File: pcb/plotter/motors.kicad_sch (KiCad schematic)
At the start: 22 parts, among them J6 Barrel_Jack_Switch, J8 Motor2, J9 Motor1, SW2 SW_SPDT, U2 bigtreetech-tmc2130, U3 bigtreetech-tmc2130, U5 MPRB2405S-6W

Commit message: PCB and 3d model. Still work in progress.
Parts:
- removed F1: Fuse, Fuse:Fuseholder_Cylinder-5x20mm_Bulgin_FX0456_Vertical_Closed, symbol Device:Fuse
- added F1: Polyfuse, Fuse:Fuse_1812_4532Metric, symbol Device:Polyfuse
- C29, C35, C37: footprint Capacitor_THT:CP_Radial_D13.0mm_P5.00mm -> Capacitor_SMD:CP_Elec_8x10
- J6: footprint Connector_BarrelJack:BarrelJack_Horizontal -> iwasz:BarrelJack_Horizontal
- J8, J9: footprint Connector_PinHeader_2.54mm:PinHeader_1x04_P2.54mm_Vertical -> Connector_JST:JST_PH_B4B-PH-K_1x04_P2.00mm_Vertical
- SW2: footprint Button_Switch_THT:SW_CuK_OS102011MA1QN1_SPDT_Angled -> iwasz:MFP 201 NR_copy
- U2, U3: footprint Module:Pololu_Breakout-16_15.2x20.3mm -> iwasz:Pololu_Breakout-16_15.2x20.3mm
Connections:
- net VDD is gone; now on net +5V: C2.2, C3.2, C30.2, C31.2, U2.2 (VDD), U3.2 (VDD)
- net +24V: now also F1.1
- net at C37.1, U5.2 (Vin): now also F1.2
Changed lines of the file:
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@@
     (pin "1")
   )
-  (symbol (lib_id "power:VDD") (at 118.745 52.07 0) (unit 1)
-    (in_bom yes) (on_board yes) (fields_autoplaced)
-    (property "Reference" "#PWR0107" (id 0) (at 118.745 55.88 0)
-      (effects (font (size 1.27 1.27)) hide)
-    )
-    (property "Value" "VDD" (id 1) (at 120.1421 51.4695 0)
+  (symbol (lib_id "power:+5V") (at 118.745 52.07 0) (unit 1)
+    (in_bom yes) (on_board yes) (fields_autoplaced)
+    (property "Reference" "#PWR?" (id 0) (at 118.745 55.88 0)
+      (effects (font (size 1.27 1.27)) hide)
+    )
+    (property "Value" "+5V" (id 1) (at 120.1421 51.4695 0)
       (effects (font (size 1.27 1.27)) (justify left))
     )
@@
     (pin "1")
   )
-  (symbol (lib_id "power:VDD") (at 173.355 52.07 0) (unit 1)
-    (in_bom yes) (on_board yes) (fields_autoplaced)
-    (property "Reference" "#PWR0104" (id 0) (at 173.355 55.88 0)
-      (effects (font (size 1.27 1.27)) hide)
-    )
-    (property "Value" "VDD" (id 1) (at 174.7521 51.4695 0)
+  (symbol (lib_id "power:+5V") (at 173.355 52.07 0) (unit 1)
+    (in_bom yes) (on_board yes) (fields_autoplaced)
+    (property "Reference" "#PWR?" (id 0) (at 173.355 55.88 0)
+      (effects (font (size 1.27 1.27)) hide)
+    )
+    (property "Value" "+5V" (id 1) (at 174.7521 51.4695 0)
       (effects (font (size 1.27 1.27)) (justify left))
     )
@@
     (pin "1")
   )
-  (symbol (lib_id "Device:Fuse") (at 104.14 166.37 90) (unit 1)
-    (in_bom yes) (on_board yes) (fields_autoplaced)
-    (property "Reference" "F1" (id 0) (at 104.14 161.6414 90))
-    (property "Value" "Fuse" (id 1) (at 104.14 164.4165 90))
-    (property "Footprint" "Fuse:Fuseholder_Cylinder-5x20mm_Bulgin_FX0456_Vertical_Closed" (id 2) (at 104.14 168.148 90)
-      (effects (font (size 1.27 1.27)) hide)
+  (symbol (lib_id "Device:Polyfuse") (at 104.14 166.37 90) (unit 1)
+    (in_bom yes) (on_board yes) (fields_autoplaced)
+    (property "Reference" "F1" (id 0) (at 104.14 161.0064 90))
+    (property "Value" "Polyfuse" (id 1) (at 104.14 163.7815 90))
+    (property "Footprint" "Fuse:Fuse_1812_4532Metric" (id 2) (at 109.22 165.1 0)
+      (effects (font (size 1.27 1.27)) (justify left) hide)
     )
     (property "Datasheet" "~" (id 3) (at 104.14 166.37 0)
@@
       (effects (font (size 1.27 1.27)) (justify left))
     )
-    (property "Footprint" "Capacitor_THT:CP_Radial_D13.0mm_P5.00mm" (id 2) (at 112.0902 175.26 0)
+    (property "Footprint" "Capacitor_SMD:CP_Elec_8x10" (id 2) (at 112.0902 175.26 0)
       (effects (font (size 1.27 1.27)) hide)
     )
@@
       (effects (font (size 1.27 1.27)) (justify left))
     )
-    (property "Footprint" "Capacitor_THT:CP_Radial_D13.0mm_P5.00mm" (id 2) (at 152.7302 64.135 0)
+    (property "Footprint" "Capacitor_SMD:CP_Elec_8x10" (id 2) (at 152.7302 64.135 0)
       (effects (font (size 1.27 1.27)) hide)
     )
@@
       (effects (font (size 1.27 1.27)) (justify left))
     )
-    (property "Footprint" "Capacitor_THT:CP_Radial_D13.0mm_P5.00mm" (id 2) (at 207.3402 64.135 0)
+    (property "Footprint" "Capacitor_SMD:CP_Elec_8x10" (id 2) (at 207.3402 64.135 0)
       (effects (font (size 1.27 1.27)) hide)
     )
@@
       (effects (font (size 1.27 1.27)) (justify right))
     )
-    (property "Footprint" "Connector_PinHeader_2.54mm:PinHeader_1x04_P2.54mm_Vertical" (id 2) (at 139.065 89.535 0)
+    (property "Footprint" "Connector_JST:JST_PH_B4B-PH-K_1x04_P2.00mm_Vertical" (id 2) (at 139.065 89.535 0)
       (effects (font (size 1.27 1.27)) hide)
     )
@@
       (effects (font (size 1.27 1.27)) (justify right))
     )
-    (property "Footprint" "Connector_PinHeader_2.54mm:PinHeader_1x04_P2.54mm_Vertical" (id 2) (at 193.675 89.535 0)
+    (property "Footprint" "Connector_JST:JST_PH_B4B-PH-K_1x04_P2.00mm_Vertical" (id 2) (at 193.675 89.535 0)
       (effects (font (size 1.27 1.27)) hide)
     )
@@
     (property "Reference" "SW2" (id 0) (at 59.69 156.9424 0))
     (property "Value" "SW_SPDT" (id 1) (at 59.69 159.7175 0))
-    (property "Footprint" "Button_Switch_THT:SW_CuK_OS102011MA1QN1_SPDT_Angled" (id 2) (at 59.69 163.83 0)
+    (property "Footprint" "iwasz:MFP 201 NR_copy" (id 2) (at 59.69 163.83 0)
       (effects (font (size 1.27 1.27)) hide)
     )
@@
     (property "Reference" "J6" (id 0) (at 42.672 158.5934 0))
     (property "Value" "Barrel_Jack_Switch" (id 1) (at 42.672 161.3685 0))
-    (property "Footprint" "Connector_BarrelJack:BarrelJack_Horizontal" (id 2) (at 42.545 167.386 0)
+    (property "Footprint" "iwasz:BarrelJack_Horizontal" (id 2) (at 42.545 167.386 0)
       (effects (font (size 1.27 1.27)) hide)
     )
@@
     (property "Reference" "U2" (id 0) (at 120.015 64.9944 0))
     (property "Value" "bigtreetech-tmc2130" (id 1) (at 120.015 67.7695 0))
-    (property "Footprint" "Module:Pololu_Breakout-16_15.2x20.3mm" (id 2) (at 120.015 88.265 0)
+    (property "Footprint" "iwasz:Pololu_Breakout-16_15.2x20.3mm" (id 2) (at 120.015 88.265 0)
       (effects (font (size 1.27 1.27)) hide)
     )
@@
     (property "Reference" "U3" (id 0) (at 174.625 64.9944 0))
     (property "Value" "bigtreetech-tmc2130" (id 1) (at 174.625 67.7695 0))
-    (property "Footprint" "Module:Pololu_Breakout-16_15.2x20.3mm" (id 2) (at 174.625 88.265 0)
-      (effects (font (size 1.27 1.27)) hide)
-    )
+    (property "Footprint" "iwasz:Pololu_Breakout-16_15.2x20.3mm" (id 2) (at 174.625 88.265 0)
+      (effects (font (size 1.27 1.27)) hide)
+    )

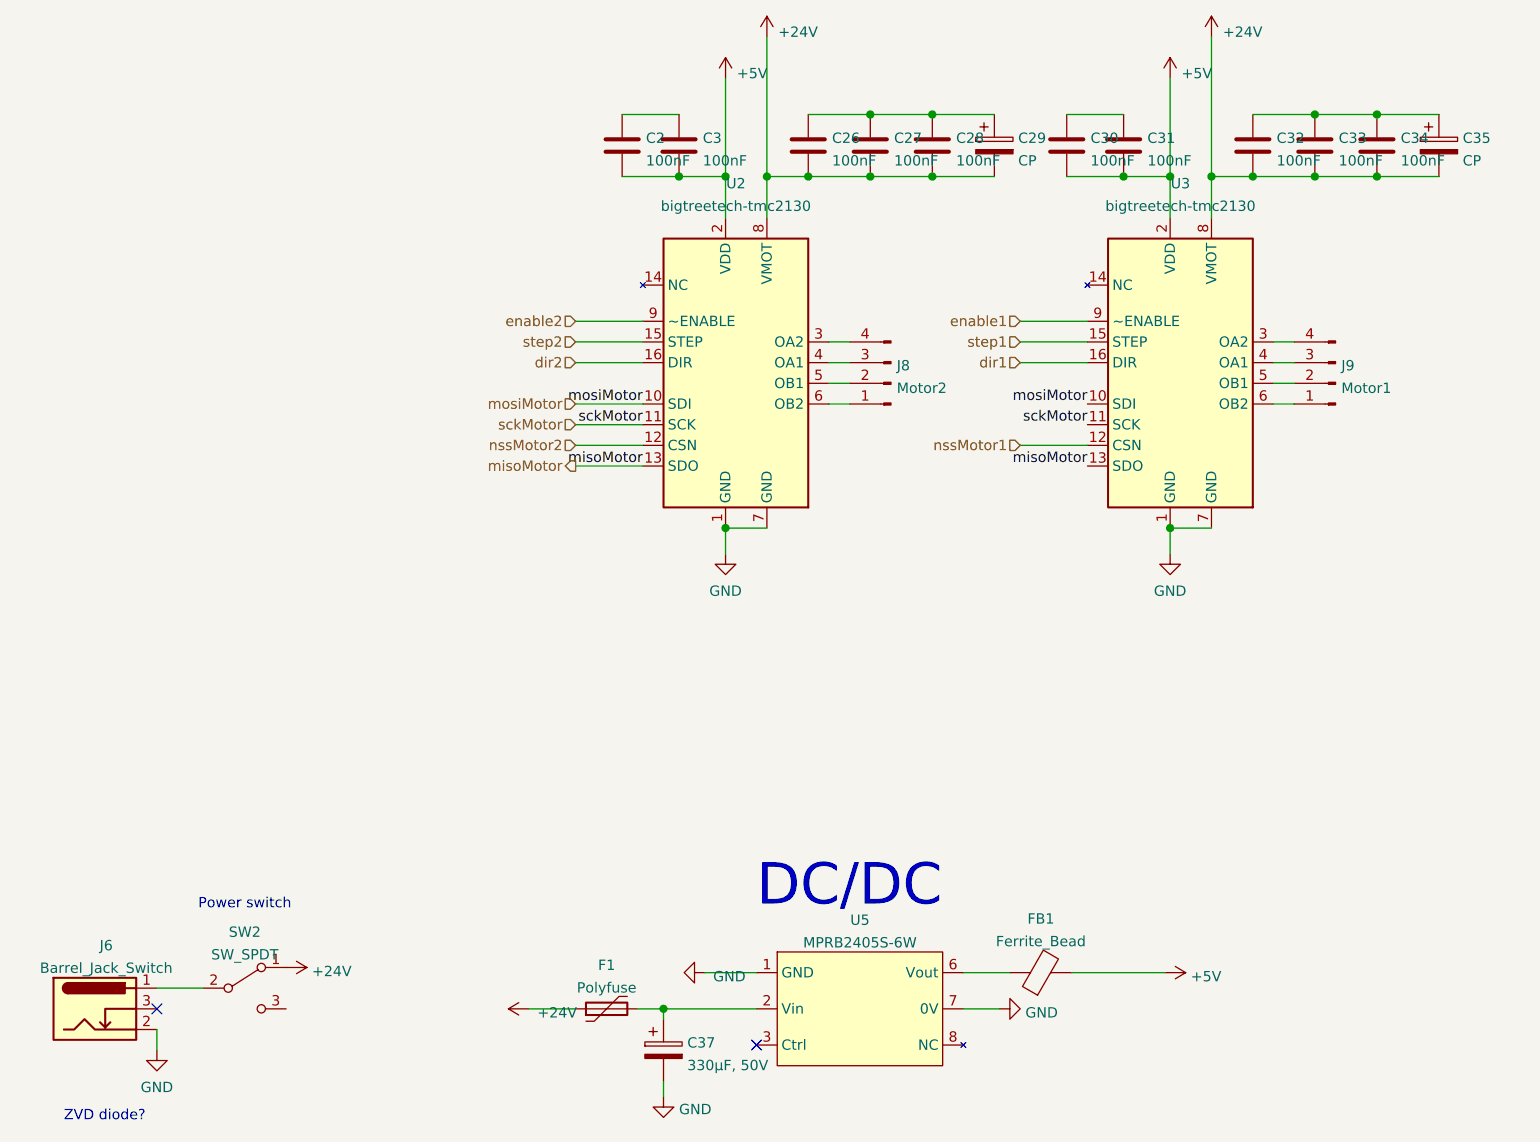
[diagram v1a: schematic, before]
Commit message: Thread priorites.
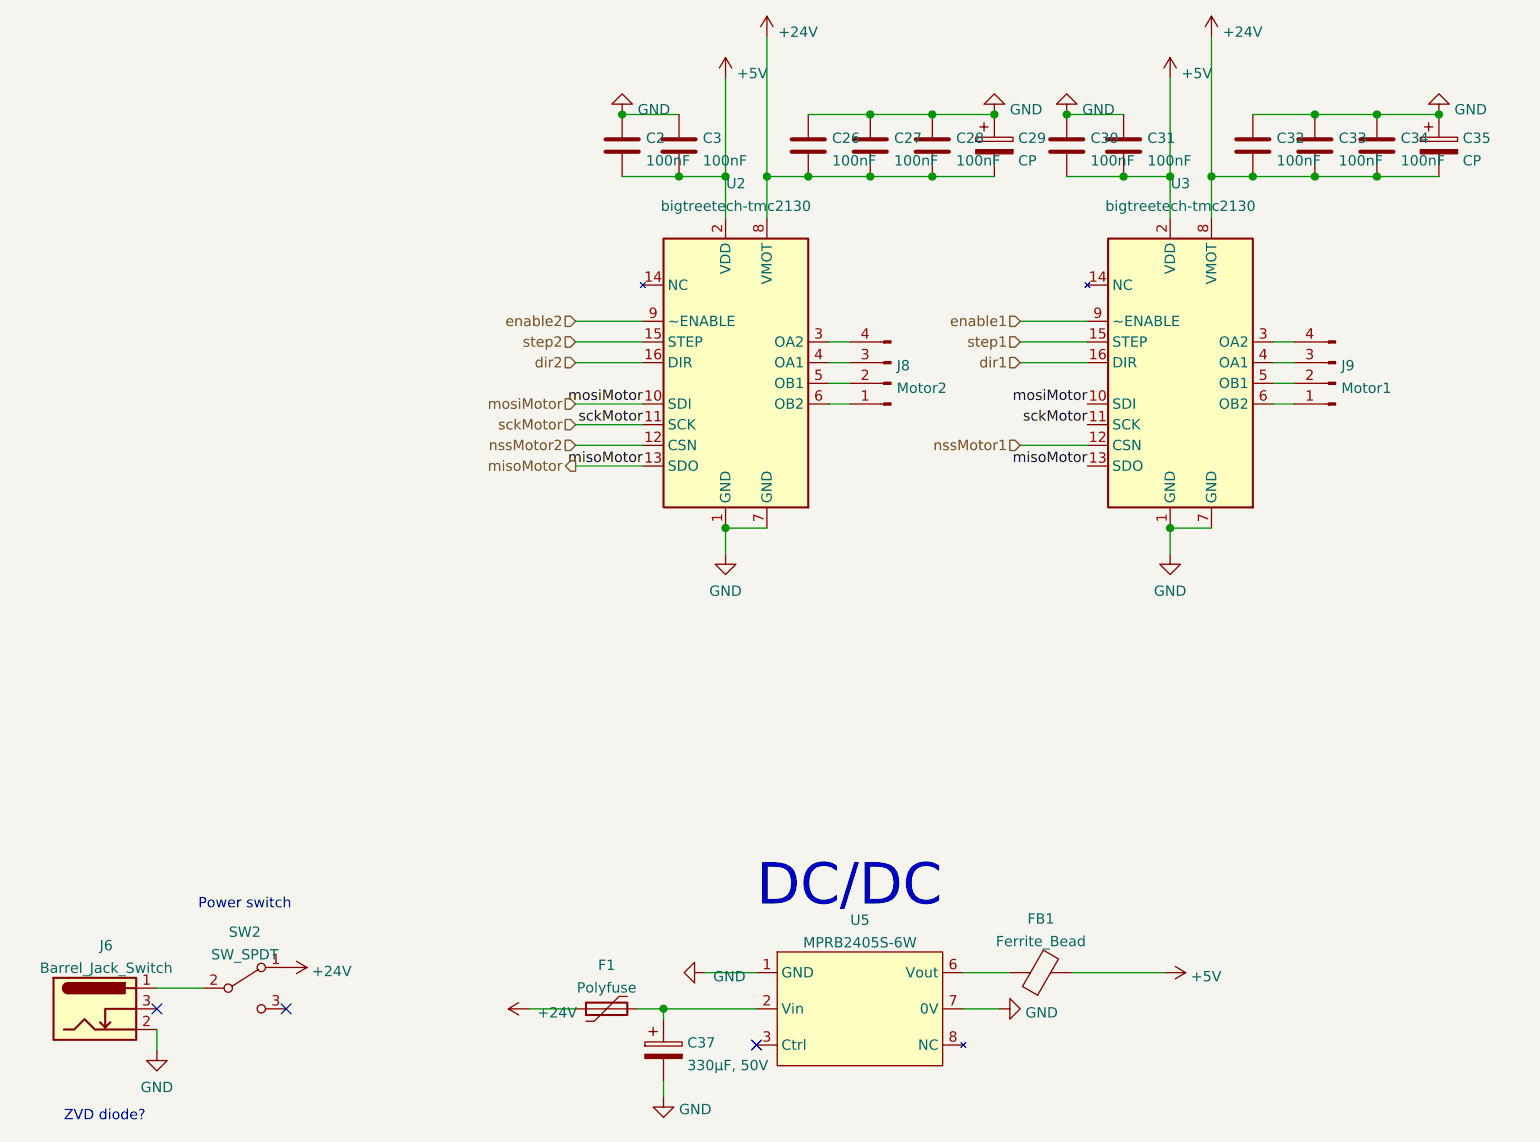
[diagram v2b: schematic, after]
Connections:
- net GND: now also C2.1, C26.1, C27.1, C28.1, C29.1, C3.1, C30.1, C31.1, C32.1, C33.1, C34.1, C35.1
- no-connect marks 2 -> 3
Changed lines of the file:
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@@
 (kicad_sch (version 20210621) (generator eeschema)
   (paper "A4")
+  (junction (at 106.045 56.515) (diameter 1.016) (color 0 0 0 0))
   (junction (at 111.125 166.37) (diameter 1.016) (color 0 0 0 0))
   (junction (at 113.03 64.135) (diameter 1.016) (color 0 0 0 0))
@@
   (junction (at 144.145 56.515) (diameter 1.016) (color 0 0 0 0))
   (junction (at 144.145 64.135) (diameter 1.016) (color 0 0 0 0))
+  (junction (at 151.765 56.515) (diameter 1.016) (color 0 0 0 0))
+  (junction (at 160.655 56.515) (diameter 1.016) (color 0 0 0 0))
   (junction (at 167.64 64.135) (diameter 1.016) (color 0 0 0 0))
   (junction (at 173.355 64.135) (diameter 1.016) (color 0 0 0 0))
@@
   (junction (at 198.755 56.515) (diameter 1.016) (color 0 0 0 0))
   (junction (at 198.755 64.135) (diameter 1.016) (color 0 0 0 0))
+  (junction (at 206.375 56.515) (diameter 1.016) (color 0 0 0 0))
   (no_connect (at 48.895 166.37))
+  (no_connect (at 64.77 166.37))
   (no_connect (at 122.555 170.815))
   (wire (pts (xy 48.895 163.83) (xy 54.61 163.83))
@@
   (symbol (lib_id "power:+5V") (at 118.745 52.07 0) (unit 1)
     (in_bom yes) (on_board yes) (fields_autoplaced)
-    (property "Reference" "#PWR?" (id 0) (at 118.745 55.88 0)
+    (property "Reference" "#PWR0104" (id 0) (at 118.745 55.88 0)
       (effects (font (size 1.27 1.27)) hide)
     )
@@
   (symbol (lib_id "power:+5V") (at 173.355 52.07 0) (unit 1)
     (in_bom yes) (on_board yes) (fields_autoplaced)
-    (property "Reference" "#PWR?" (id 0) (at 173.355 55.88 0)
+    (property "Reference" "#PWR0107" (id 0) (at 173.355 55.88 0)
       (effects (font (size 1.27 1.27)) hide)
     )
@@
     (pin "1")
   )
+  (symbol (lib_id "power:GND") (at 106.045 56.515 180) (unit 1)
+    (in_bom yes) (on_board yes) (fields_autoplaced)
+    (property "Reference" "#PWR022" (id 0) (at 106.045 50.165 0)
+      (effects (font (size 1.27 1.27)) hide)
+    )
+    (property "Value" "GND" (id 1) (at 107.9501 55.9145 0)
+      (effects (font (size 1.27 1.27)) (justify right))
+    )
+    (property "Footprint" "" (id 2) (at 106.045 56.515 0)
+      (effects (font (size 1.27 1.27)) hide)
+    )
+    (property "Datasheet" "" (id 3) (at 106.045 56.515 0)
+      (effects (font (size 1.27 1.27)) hide)
+    )
+    (pin "1")
+  )
   (symbol (lib_id "power:GND") (at 111.125 177.165 0) (unit 1)
     (in_bom yes) (on_board yes) (fields_autoplaced)
@@
     (pin "1")
   )
+  (symbol (lib_id "power:GND") (at 151.765 56.515 180) (unit 1)
+    (in_bom yes) (on_board yes) (fields_autoplaced)
+    (property "Reference" "#PWR023" (id 0) (at 151.765 50.165 0)
+      (effects (font (size 1.27 1.27)) hide)
+    )
+    (property "Value" "GND" (id 1) (at 153.6701 55.9145 0)
+      (effects (font (size 1.27 1.27)) (justify right))
+    )
+    (property "Footprint" "" (id 2) (at 151.765 56.515 0)
+      (effects (font (size 1.27 1.27)) hide)
+    )
+    (property "Datasheet" "" (id 3) (at 151.765 56.515 0)
+      (effects (font (size 1.27 1.27)) hide)
+    )
+    (pin "1")
+  )
   (symbol (lib_id "power:GND") (at 152.4 166.37 90) (unit 1)
     (in_bom yes) (on_board yes) (fields_autoplaced)
@@
     (pin "1")
   )
+  (symbol (lib_id "power:GND") (at 160.655 56.515 180) (unit 1)
+    (in_bom yes) (on_board yes) (fields_autoplaced)
+    (property "Reference" "#PWR024" (id 0) (at 160.655 50.165 0)
+      (effects (font (size 1.27 1.27)) hide)
+    )
+    (property "Value" "GND" (id 1) (at 162.5601 55.9145 0)
+      (effects (font (size 1.27 1.27)) (justify right))
+    )
+    (property "Footprint" "" (id 2) (at 160.655 56.515 0)
+      (effects (font (size 1.27 1.27)) hide)
+    )
+    (property "Datasheet" "" (id 3) (at 160.655 56.515 0)
+      (effects (font (size 1.27 1.27)) hide)
+    )
+    (pin "1")
+  )
   (symbol (lib_id "power:GND") (at 173.355 110.49 0) (unit 1)
     (in_bom yes) (on_board yes) (fields_autoplaced)
@@
       (effects (font (size 1.27 1.27)) hide)
     )
+    (pin "1")
+  )
+  (symbol (lib_id "power:GND") (at 206.375 56.515 180) (unit 1)
+    (in_bom yes) (on_board yes) (fields_autoplaced)
+    (property "Reference" "#PWR025" (id 0) (at 206.375 50.165 0)
+      (effects (font (size 1.27 1.27)) hide)
+    )
+    (property "Value" "GND" (id 1) (at 208.2801 55.9145 0)
+      (effects (font (size 1.27 1.27)) (justify right))
+    )
+    (property "Footprint" "" (id 2) (at 206.375 56.515 0)
+      (effects (font (size 1.27 1.27)) hide)
+    )
+    (property "Datasheet" "" (id 3) (at 206.375 56.515 0)
+      (effects (font (size 1.27 1.27)) hide)
+    )

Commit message: Bringing up the first PCB
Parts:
- C29, C35: value CP -> 100µF
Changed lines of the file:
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@@
       (effects (font (size 1.27 1.27)) (justify left))
     )
-    (property "Value" "CP" (id 1) (at 154.6861 62.1916 0)
+    (property "Value" "100µF" (id 1) (at 154.6861 62.1916 0)
       (effects (font (size 1.27 1.27)) (justify left))
     )
@@
       (effects (font (size 1.27 1.27)) (justify left))
     )
-    (property "Value" "CP" (id 1) (at 209.2961 62.1916 0)
+    (property "Value" "100µF" (id 1) (at 209.2961 62.1916 0)
       (effects (font (size 1.27 1.27)) (justify left))
     )

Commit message: Schematics minor changes
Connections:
- net +24V: now also C29.1, C35.1; no longer C29.2, C35.2
- net GND: now also C29.2, C35.2; no longer C29.1, C35.1
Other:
- moved on the sheet: C29, C35
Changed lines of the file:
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@@
     (pin "2")
   )
-  (symbol (lib_id "Device:CP") (at 151.765 60.325 0) (unit 1)
+  (symbol (lib_id "Device:CP") (at 151.765 60.325 180) (unit 1)
     (in_bom yes) (on_board yes) (fields_autoplaced)
     (property "Reference" "C29" (id 0) (at 154.6861 59.4165 0)
-      (effects (font (size 1.27 1.27)) (justify left))
+      (effects (font (size 1.27 1.27)) (justify right))
     )
     (property "Value" "100µF" (id 1) (at 154.6861 62.1916 0)
-      (effects (font (size 1.27 1.27)) (justify left))
+      (effects (font (size 1.27 1.27)) (justify right))
     )
-    (property "Footprint" "Capacitor_SMD:CP_Elec_8x10" (id 2) (at 152.7302 64.135 0)
+    (property "Footprint" "Capacitor_SMD:CP_Elec_8x10" (id 2) (at 150.7998 56.515 0)
       (effects (font (size 1.27 1.27)) hide)
     )
@@
     (pin "2")
   )
-  (symbol (lib_id "Device:CP") (at 206.375 60.325 0) (unit 1)
+  (symbol (lib_id "Device:CP") (at 206.375 60.325 180) (unit 1)
     (in_bom yes) (on_board yes) (fields_autoplaced)
     (property "Reference" "C35" (id 0) (at 209.2961 59.4165 0)
-      (effects (font (size 1.27 1.27)) (justify left))
+      (effects (font (size 1.27 1.27)) (justify right))
     )
     (property "Value" "100µF" (id 1) (at 209.2961 62.1916 0)
-      (effects (font (size 1.27 1.27)) (justify left))
+      (effects (font (size 1.27 1.27)) (justify right))
     )
-    (property "Footprint" "Capacitor_SMD:CP_Elec_8x10" (id 2) (at 207.3402 64.135 0)
+    (property "Footprint" "Capacitor_SMD:CP_Elec_8x10" (id 2) (at 205.4098 56.515 0)
       (effects (font (size 1.27 1.27)) hide)
     )

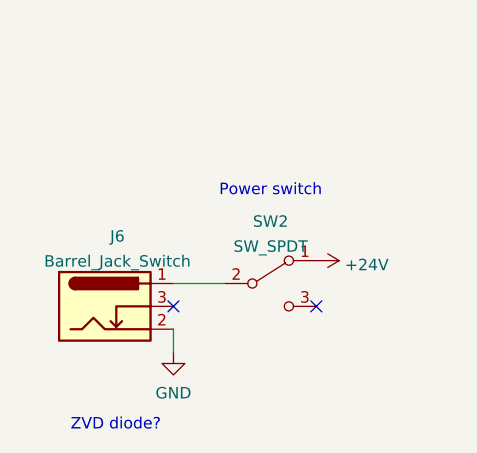
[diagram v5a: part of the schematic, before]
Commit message: Steppers config upudated
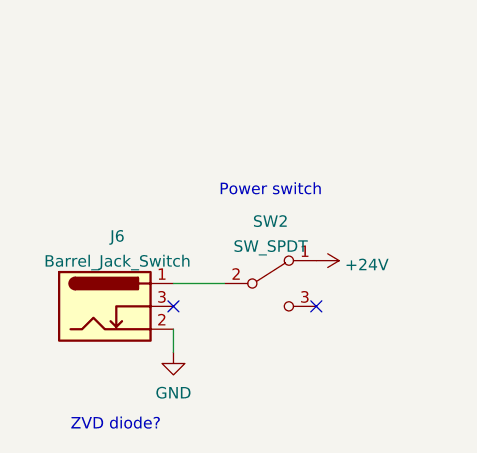
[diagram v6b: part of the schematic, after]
